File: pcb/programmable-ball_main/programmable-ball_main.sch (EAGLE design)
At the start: 1 part, among them U1 MDBT50Q-1MV2

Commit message: 軽微な修正 #4
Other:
- moved on the sheet: U1
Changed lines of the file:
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@@
 <attribute name="SHEET" x="368.3" y="4.445" size="2.54" layer="94" font="vector"/>
 </instance>
-<instance part="U1" gate="G$1" x="226.06" y="190.5" smashed="yes">
-<attribute name="NAME" x="203.2" y="236.982" size="1.778" layer="95"/>
-<attribute name="VALUE" x="200.66" y="139.7" size="1.778" layer="96"/>
+<instance part="U1" gate="G$1" x="246.38" y="187.96" smashed="yes">
+<attribute name="NAME" x="223.52" y="234.442" size="1.778" layer="95"/>
+<attribute name="VALUE" x="223.52" y="139.7" size="1.778" layer="96"/>
 </instance>
 </instances>

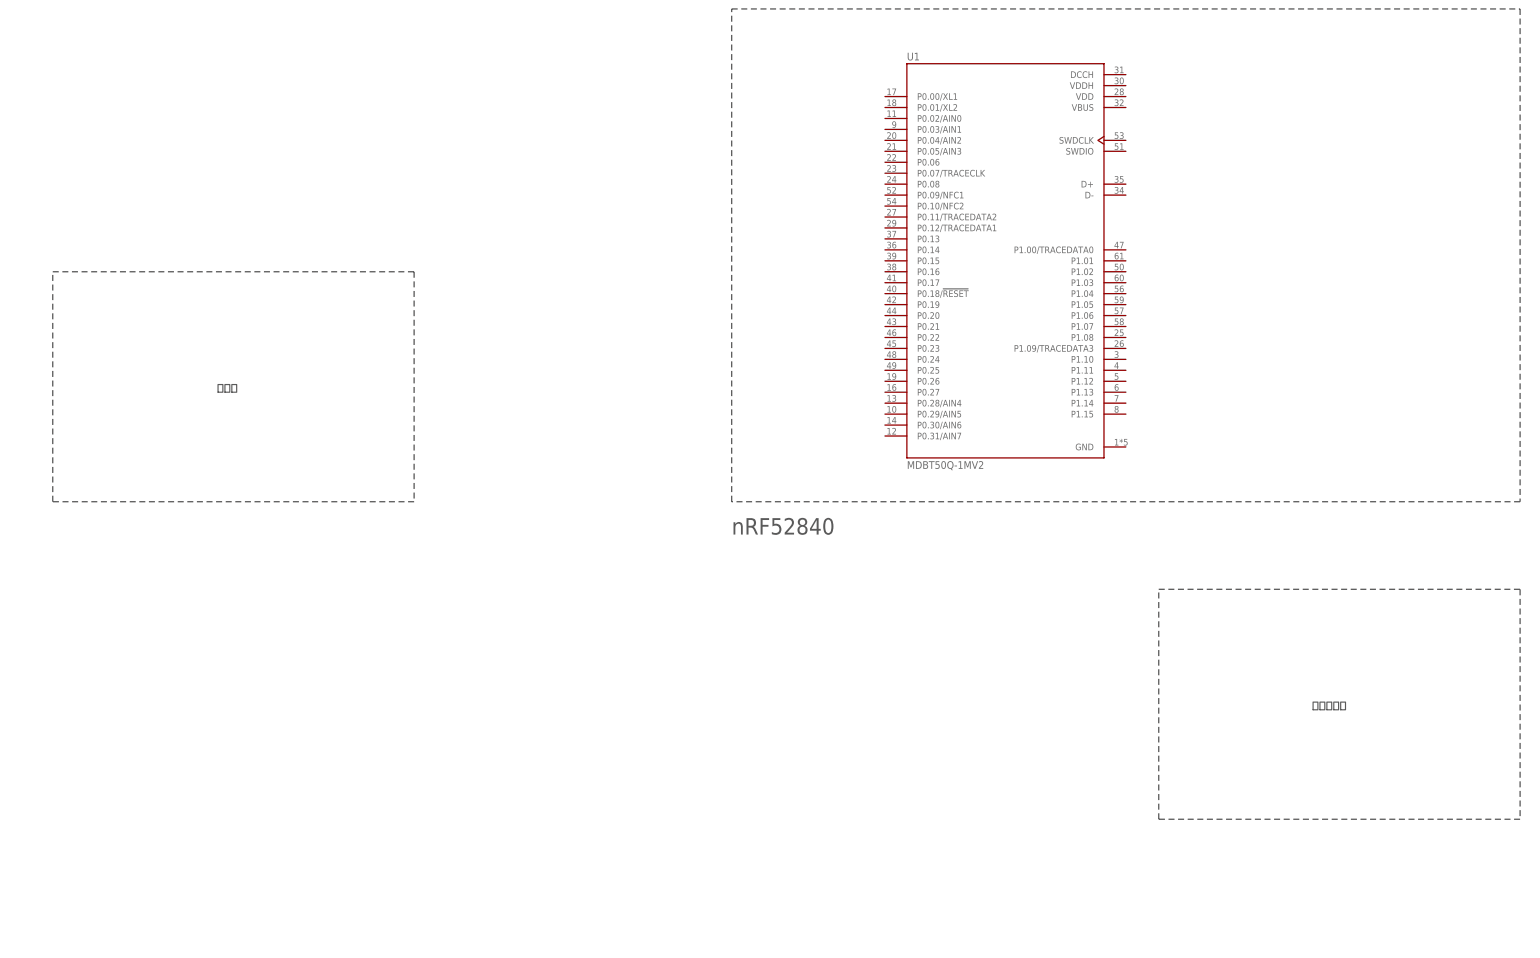
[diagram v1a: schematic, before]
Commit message: Added Circular Board and TypeC Connector #4
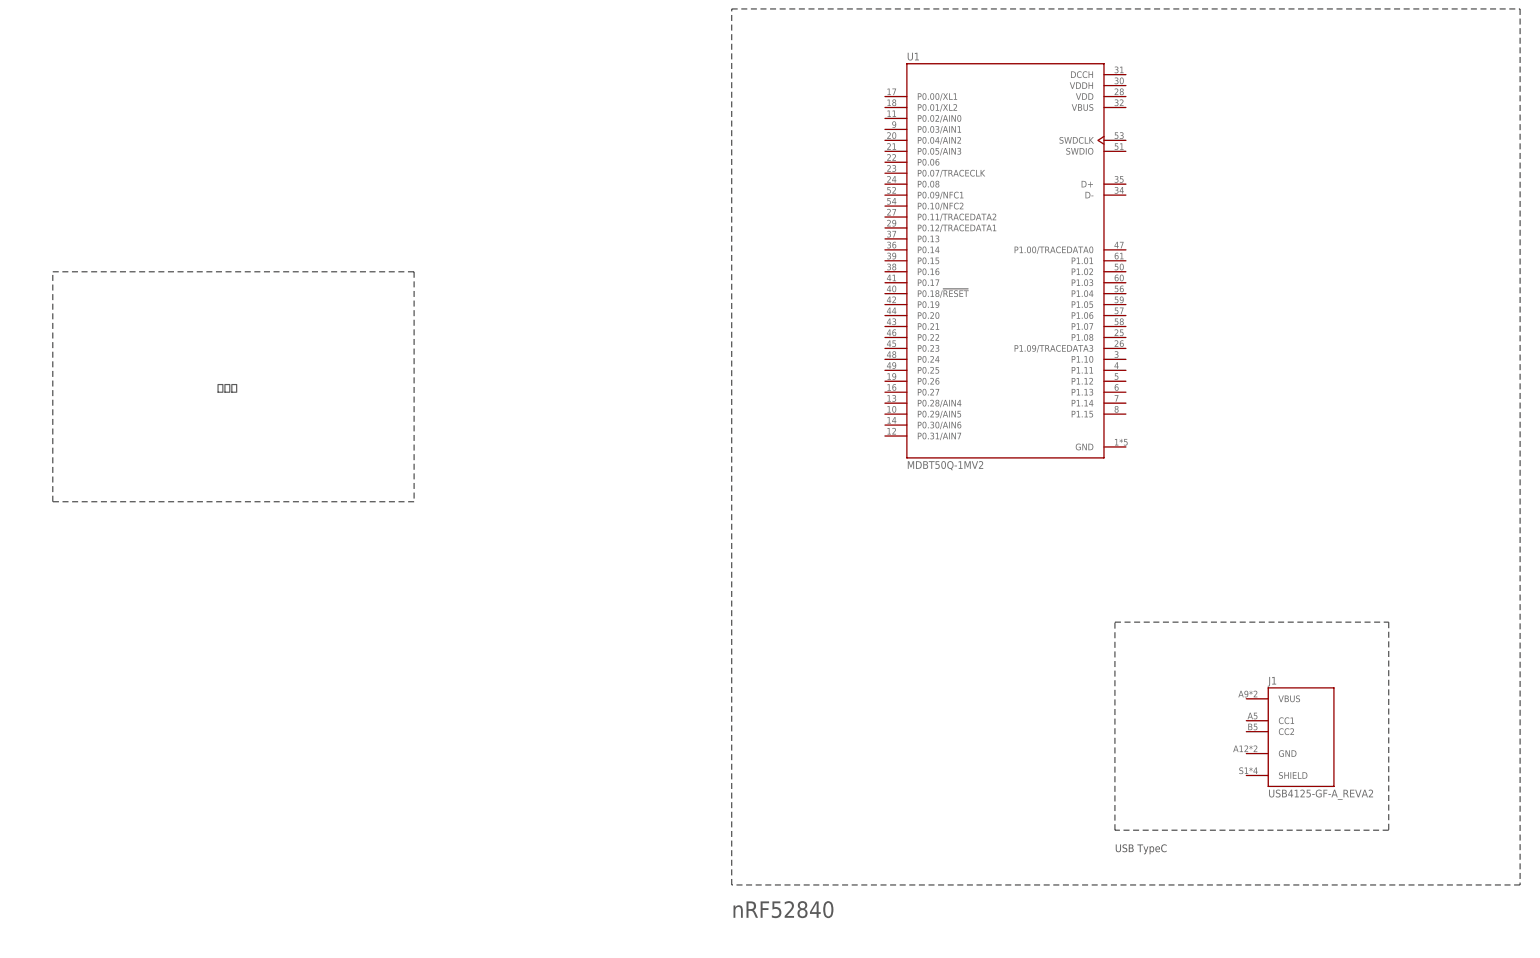
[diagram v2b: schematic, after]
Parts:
- added J1: USB4125-GF-A_REVA2, USB4125-GF-A_REVA2:USB4125-GF-A_REVA2
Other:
- note added: "USB TypeC"
- note removed: "コネクタ系"
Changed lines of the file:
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@@
 <part name="FRAME1" library="SparkFun-Retired" deviceset="FRAME-A3" device=""/>
 <part name="U1" library="MDBT50Q-1MV2" deviceset="MDBT50Q-1MV2" device=""/>
+<part name="J1" library="USB4125-GF-A_REVA2" deviceset="USB4125-GF-A_REVA2" device=""/>
 </parts>
 <sheets>
 <sheet>
 <plain>
-<wire x1="365.76" y1="132.08" x2="182.88" y2="132.08" width="0.1524" layer="97" style="shortdash"/>
-<wire x1="182.88" y1="132.08" x2="182.88" y2="246.38" width="0.1524" layer="97" style="shortdash"/>
+<wire x1="365.76" y1="43.18" x2="182.88" y2="43.18" width="0.1524" layer="97" style="shortdash"/>
+<wire x1="182.88" y1="43.18" x2="182.88" y2="246.38" width="0.1524" layer="97" style="shortdash"/>
 <wire x1="182.88" y1="246.38" x2="365.76" y2="246.38" width="0.1524" layer="97" style="shortdash"/>
-<wire x1="365.76" y1="246.38" x2="365.76" y2="132.08" width="0.1524" layer="97" style="shortdash"/>
-<text x="182.88" y="124.46" size="3.81" layer="97">nRF52840</text>
+<wire x1="365.76" y1="246.38" x2="365.76" y2="43.18" width="0.1524" layer="97" style="shortdash"/>
+<text x="182.88" y="35.56" size="3.81" layer="97">nRF52840</text>
 <wire x1="25.4" y1="185.42" x2="109.22" y2="185.42" width="0.1524" layer="97" style="shortdash"/>
 <wire x1="109.22" y1="185.42" x2="109.22" y2="132.08" width="0.1524" layer="97" style="shortdash"/>
@@
 <wire x1="25.4" y1="132.08" x2="25.4" y2="185.42" width="0.1524" layer="97" style="shortdash"/>
 <text x="63.5" y="157.48" size="1.778" layer="97">電源系</text>
-<wire x1="281.94" y1="111.76" x2="365.76" y2="111.76" width="0.1524" layer="97" style="shortdash"/>
-<wire x1="365.76" y1="111.76" x2="365.76" y2="58.42" width="0.1524" layer="97" style="shortdash"/>
-<wire x1="365.76" y1="58.42" x2="281.94" y2="58.42" width="0.1524" layer="97" style="shortdash"/>
-<wire x1="281.94" y1="58.42" x2="281.94" y2="111.76" width="0.1524" layer="97" style="shortdash"/>
-<text x="317.5" y="83.82" size="1.778" layer="97">コネクタ系</text>
+<wire x1="271.78" y1="104.14" x2="335.28" y2="104.14" width="0.1524" layer="97" style="shortdash"/>
+<wire x1="335.28" y1="104.14" x2="335.28" y2="55.88" width="0.1524" layer="97" style="shortdash"/>
+<wire x1="335.28" y1="55.88" x2="271.78" y2="55.88" width="0.1524" layer="97" style="shortdash"/>
+<wire x1="271.78" y1="55.88" x2="271.78" y2="104.14" width="0.1524" layer="97" style="shortdash"/>
+<text x="271.78" y="50.8" size="1.778" layer="97">USB TypeC</text>
 </plain>
 <instances>
@@
 <attribute name="VALUE" x="223.52" y="139.7" size="1.778" layer="96"/>
 </instance>
+<instance part="J1" gate="G$1" x="314.96" y="78.74" smashed="yes">
+<attribute name="NAME" x="307.34" y="89.662" size="1.778" layer="95"/>
+<attribute name="VALUE" x="307.34" y="65.278" size="1.778" layer="96" rot="MR180"/>
+</instance>
 </instances>

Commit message: 軽微な修正
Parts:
- J1: value USB4125-GF-A_REVA2 -> USB4056-03-A_REVA2; device USB4125-GF-A_REVA2:USB4125-GF-A_REVA2 -> USB4056-03-A_REVA2:USB4056-03-A_REVA2
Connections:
- new net GND: U1.GND
- new net USBD+: U1.D+
- new net USBD-: U1.D-
- new net VBUS: U1.VBUS
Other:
- note added: "fixme : typc-c usbd+も出せるようにして"
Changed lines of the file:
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@@
 <layers>
 <layer number="1" name="Top" color="4" fill="1" visible="no" active="no"/>
+<layer number="2" name="Route2" color="1" fill="3" visible="no" active="no"/>
+<layer number="3" name="Route3" color="4" fill="3" visible="no" active="no"/>
+<layer number="4" name="Route4" color="1" fill="4" visible="no" active="no"/>
+<layer number="5" name="Route5" color="4" fill="4" visible="no" active="no"/>
+<layer number="6" name="Route6" color="1" fill="8" visible="no" active="no"/>
+<layer number="7" name="Route7" color="4" fill="8" visible="no" active="no"/>
+<layer number="8" name="Route8" color="1" fill="2" visible="no" active="no"/>
+<layer number="9" name="Route9" color="4" fill="2" visible="no" active="no"/>
+<layer number="10" name="Route10" color="1" fill="7" visible="no" active="no"/>
+<layer number="11" name="Route11" color="4" fill="7" visible="no" active="no"/>
+<layer number="12" name="Route12" color="1" fill="5" visible="no" active="no"/>
+<layer number="13" name="Route13" color="4" fill="5" visible="no" active="no"/>
+<layer number="14" name="Route14" color="1" fill="6" visible="no" active="no"/>
+<layer number="15" name="Route15" color="4" fill="6" visible="no" active="no"/>
 <layer number="16" name="Bottom" color="1" fill="1" visible="no" active="no"/>
 <layer number="17" name="Pads" color="2" fill="1" visible="no" active="no"/>
@@
 <part name="FRAME1" library="SparkFun-Retired" deviceset="FRAME-A3" device=""/>
 <part name="U1" library="MDBT50Q-1MV2" deviceset="MDBT50Q-1MV2" device=""/>
-<part name="J1" library="USB4125-GF-A_REVA2" deviceset="USB4125-GF-A_REVA2" device=""/>
+<part name="GND1" library="supply1" library_urn="urn:adsk.eagle:library:371" deviceset="GND" device=""/>
+<part name="GND2" library="supply1" library_urn="urn:adsk.eagle:library:371" deviceset="GND" device=""/>
+<part name="GND3" library="supply1" library_urn="urn:adsk.eagle:library:371" deviceset="GND" device=""/>
+<part name="J1" library="USB4056-03-A_REVA2" deviceset="USB4056-03-A_REVA2" device=""/>
 </parts>
 <sheets>
 <sheet>
 <plain>
-<wire x1="365.76" y1="43.18" x2="182.88" y2="43.18" width="0.1524" layer="97" style="shortdash"/>
-<wire x1="182.88" y1="43.18" x2="182.88" y2="246.38" width="0.1524" layer="97" style="shortdash"/>
-<wire x1="182.88" y1="246.38" x2="365.76" y2="246.38" width="0.1524" layer="97" style="shortdash"/>
+<wire x1="365.76" y1="43.18" x2="165.1" y2="43.18" width="0.1524" layer="97" style="shortdash"/>
+<wire x1="165.1" y1="43.18" x2="165.1" y2="246.38" width="0.1524" layer="97" style="shortdash"/>
+<wire x1="165.1" y1="246.38" x2="365.76" y2="246.38" width="0.1524" layer="97" style="shortdash"/>
 <wire x1="365.76" y1="246.38" x2="365.76" y2="43.18" width="0.1524" layer="97" style="shortdash"/>
-<text x="182.88" y="35.56" size="3.81" layer="97">nRF52840</text>
+<text x="167.64" y="35.56" size="3.81" layer="97">nRF52840</text>
 <wire x1="25.4" y1="185.42" x2="109.22" y2="185.42" width="0.1524" layer="97" style="shortdash"/>
 <wire x1="109.22" y1="185.42" x2="109.22" y2="132.08" width="0.1524" layer="97" style="shortdash"/>
@@
 <wire x1="25.4" y1="132.08" x2="25.4" y2="185.42" width="0.1524" layer="97" style="shortdash"/>
 <text x="63.5" y="157.48" size="1.778" layer="97">電源系</text>
-<wire x1="271.78" y1="104.14" x2="335.28" y2="104.14" width="0.1524" layer="97" style="shortdash"/>
-<wire x1="335.28" y1="104.14" x2="335.28" y2="55.88" width="0.1524" layer="97" style="shortdash"/>
-<wire x1="335.28" y1="55.88" x2="271.78" y2="55.88" width="0.1524" layer="97" style="shortdash"/>
-<wire x1="271.78" y1="55.88" x2="271.78" y2="104.14" width="0.1524" layer="97" style="shortdash"/>
-<text x="271.78" y="50.8" size="1.778" layer="97">USB TypeC</text>
+<wire x1="304.8" y1="104.14" x2="355.6" y2="104.14" width="0.1524" layer="97" style="shortdash"/>
+<wire x1="355.6" y1="104.14" x2="355.6" y2="55.88" width="0.1524" layer="97" style="shortdash"/>
+<wire x1="355.6" y1="55.88" x2="304.8" y2="55.88" width="0.1524" layer="97" style="shortdash"/>
+<wire x1="304.8" y1="55.88" x2="304.8" y2="104.14" width="0.1524" layer="97" style="shortdash"/>
+<text x="309.88" y="53.34" size="1.778" layer="97">USB TypeC</text>
+<text x="304.8" y="106.68" size="1.778" layer="97">fixme : typc-c usbd+も出せるようにして</text>
+<wire x1="223.52" y1="104.14" x2="294.64" y2="104.14" width="0.1524" layer="97" style="shortdash"/>
+<wire x1="294.64" y1="104.14" x2="294.64" y2="55.88" width="0.1524" layer="97" style="shortdash"/>
+<wire x1="294.64" y1="55.88" x2="223.52" y2="55.88" width="0.1524" layer="97" style="shortdash"/>
+<wire x1="223.52" y1="55.88" x2="223.52" y2="104.14" width="0.1524" layer="97" style="shortdash"/>
+<text x="248.92" y="53.34" size="1.778" layer="97">USB TypeC</text>
+<text x="243.84" y="106.68" size="1.778" layer="97">fixme : typc-c usbd+も出せるようにして</text>
 </plain>
 <instances>
@@
 <attribute name="VALUE" x="223.52" y="139.7" size="1.778" layer="96"/>
 </instance>
-<instance part="J1" gate="G$1" x="314.96" y="78.74" smashed="yes">
-<attribute name="NAME" x="307.34" y="89.662" size="1.778" layer="95"/>
-<attribute name="VALUE" x="307.34" y="65.278" size="1.778" layer="96" rot="MR180"/>
+<instance part="GND1" gate="1" x="276.86" y="137.16" smashed="yes">
+<attribute name="VALUE" x="274.32" y="134.62" size="1.778" layer="96"/>
+</instance>
+<instance part="GND2" gate="1" x="340.36" y="63.5" smashed="yes">
+<attribute name="VALUE" x="337.82" y="60.96" size="1.778" layer="96"/>
+</instance>
+<instance part="GND3" gate="1" x="279.4" y="63.5" smashed="yes">
+<attribute name="VALUE" x="276.86" y="60.96" size="1.778" layer="96"/>
+</instance>
+<instance part="J1" gate="G$1" x="248.92" y="83.82" smashed="yes">
+<attribute name="NAME" x="236.22" y="99.822" size="1.778" layer="95"/>
+<attribute name="VALUE" x="236.22" y="65.278" size="1.778" layer="96" rot="MR180"/>
 </instance>
 </instances>
@@
 </busses>
 <nets>
+<net name="GND" class="0">
+<segment>
+<pinref part="U1" gate="G$1" pin="GND"/>
+<pinref part="GND1" gate="1" pin="GND"/>
+<wire x1="274.32" y1="144.78" x2="276.86" y2="144.78" width="0.1524" layer="91"/>
+<wire x1="276.86" y1="144.78" x2="276.86" y2="139.7" width="0.1524" layer="91"/>
+</segment>
+<segment>
+<pinref part="GND2" gate="1" pin="GND"/>
+<wire x1="330.2" y1="76.2" x2="340.36" y2="76.2" width="0.1524" layer="91"/>
+<wire x1="340.36" y1="76.2" x2="340.36" y2="66.04" width="0.1524" layer="91"/>
+</segment>
+<segment>
+<pinref part="GND3" gate="1" pin="GND"/>
+<wire x1="269.24" y1="76.2" x2="279.4" y2="76.2" width="0.1524" layer="91"/>
+<wire x1="279.4" y1="76.2" x2="279.4" y2="66.04" width="0.1524" layer="91"/>
+</segment>
+</net>
+<net name="VBUS" class="0">
+<segment>
+<pinref part="U1" gate="G$1" pin="VBUS"/>
+<wire x1="274.32" y1="223.52" x2="281.94" y2="223.52" width="0.1524" layer="91"/>
+<label x="281.94" y="223.52" size="1.27" layer="95" xref="yes"/>
+</segment>
+</net>
+<net name="USBD+" class="0">
+<segment>
+<pinref part="U1" gate="G$1" pin="D+"/>
+<wire x1="274.32" y1="205.74" x2="281.94" y2="205.74" width="0.1524" layer="91"/>
+<label x="281.94" y="205.74" size="1.27" layer="95" xref="yes"/>
+</segment>
+</net>
+<net name="USBD-" class="0">
+<segment>
+<pinref part="U1" gate="G$1" pin="D-"/>
+<wire x1="274.32" y1="203.2" x2="281.94" y2="203.2" width="0.1524" layer="91"/>
+<label x="281.94" y="203.2" size="1.27" layer="95" xref="yes"/>
+</segment>
+</net>
+<net name="N$1" class="0">
+<segment>
+<wire x1="330.2" y1="88.9" x2="340.36" y2="88.9" width="0.1524" layer="91"/>
+<wire x1="340.36" y1="88.9" x2="340.36" y2="96.52" width="0.1524" layer="91"/>
+</segment>
+</net>
+<net name="N$2" class="0">
+<segment>
+<wire x1="330.2" y1="83.82" x2="340.36" y2="83.82" width="0.1524" layer="91"/>
+</segment>
+</net>
+<net name="N$3" class="0">
+<segment>
+<wire x1="330.2" y1="81.28" x2="340.36" y2="81.28" width="0.1524" layer="91"/>
+</segment>
+</net>
+<net name="N$4" class="0">
+<segment>
+<wire x1="269.24" y1="88.9" x2="279.4" y2="88.9" width="0.1524" layer="91"/>
+<wire x1="279.4" y1="88.9" x2="279.4" y2="96.52" width="0.1524" layer="91"/>
+</segment>
+</net>
+<net name="N$5" class="0">
+<segment>
+<wire x1="269.24" y1="83.82" x2="279.4" y2="83.82" width="0.1524" layer="91"/>
+</segment>
+</net>
+<net name="N$6" class="0">
+<segment>
+<wire x1="269.24" y1="81.28" x2="279.4" y2="81.28" width="0.1524" layer="91"/>
+</segment>
+</net>
 </nets>
 </sheet>
@@
 </schematic>
 </drawing>
+<compatibility>
+<note version="8.2" severity="warning">
+Since Version 8.2, EAGLE supports online libraries. The ids
+of those online libraries will not be understood (or retained)
+with this version.
+</note>
+<note version="8.3" severity="warning">
+Since Version 8.3, EAGLE supports URNs for individual library
+assets (packages, symbols, and devices). The URNs of those assets
+will not be understood (or retained) with this version.
+</note>
+</compatibility>
 </eagle>

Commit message: usb typeC周り実装 #4
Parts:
- added R1, R2: 5.1k, SparkFun-Resistors:5.1KOHM-0402T-1/16W-1%
- J1: value USB4056-03-A_REVA2 -> 12402012E212A; device USB4056-03-A_REVA2:USB4056-03-A_REVA2 -> 12402012E212A:12402012E212A
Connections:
- new net N$1: J1.CC1_A, R1.2
- new net N$2: J1.CC1_B, R2.2
- net GND: now also J1.GND, R1.1, R2.1
- net USBD+: now also J1.D+_A, J1.D+_B
- net USBD-: now also J1.D-_A, J1.D-_B
- net VBUS: now also J1.VBUS
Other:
- note added: "I2C Connector"
- note removed: "fixme : typc-c usbd+も出せるようにして"
- moved on the sheet: U1
